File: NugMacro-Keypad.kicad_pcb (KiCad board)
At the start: 2 copper layers, 76.2 x 97.2 mm, 51 parts, among them J2 Conn_01x04, J3 Conn_01x04_Female_For_LCD, SW1 SW_Push, SW2 RotaryEncoder_Switch, U1 ATmega32U4-A, Y1 16MHz

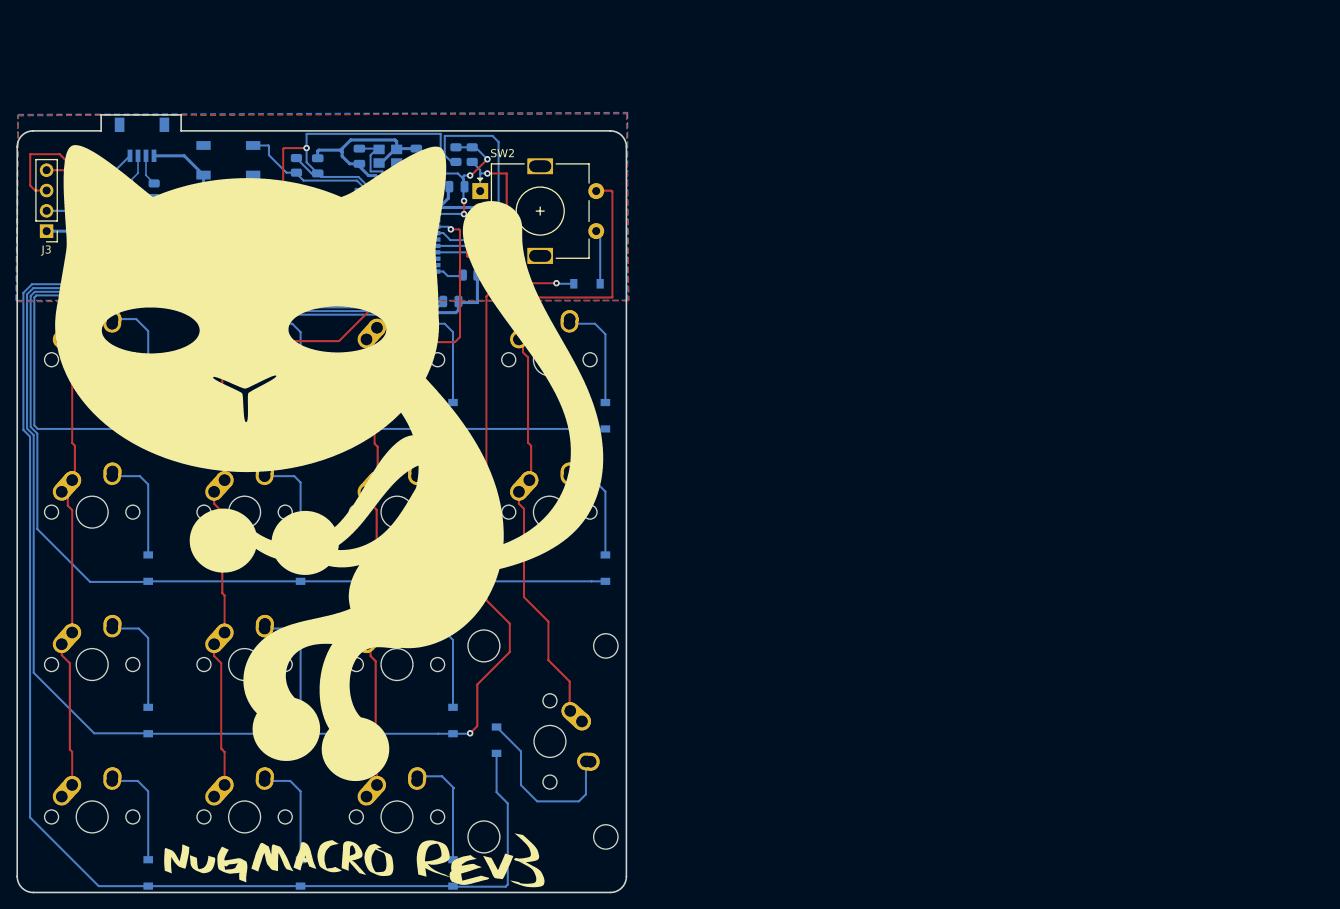
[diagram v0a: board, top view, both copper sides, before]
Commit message: ssilkcreen changess
added cat
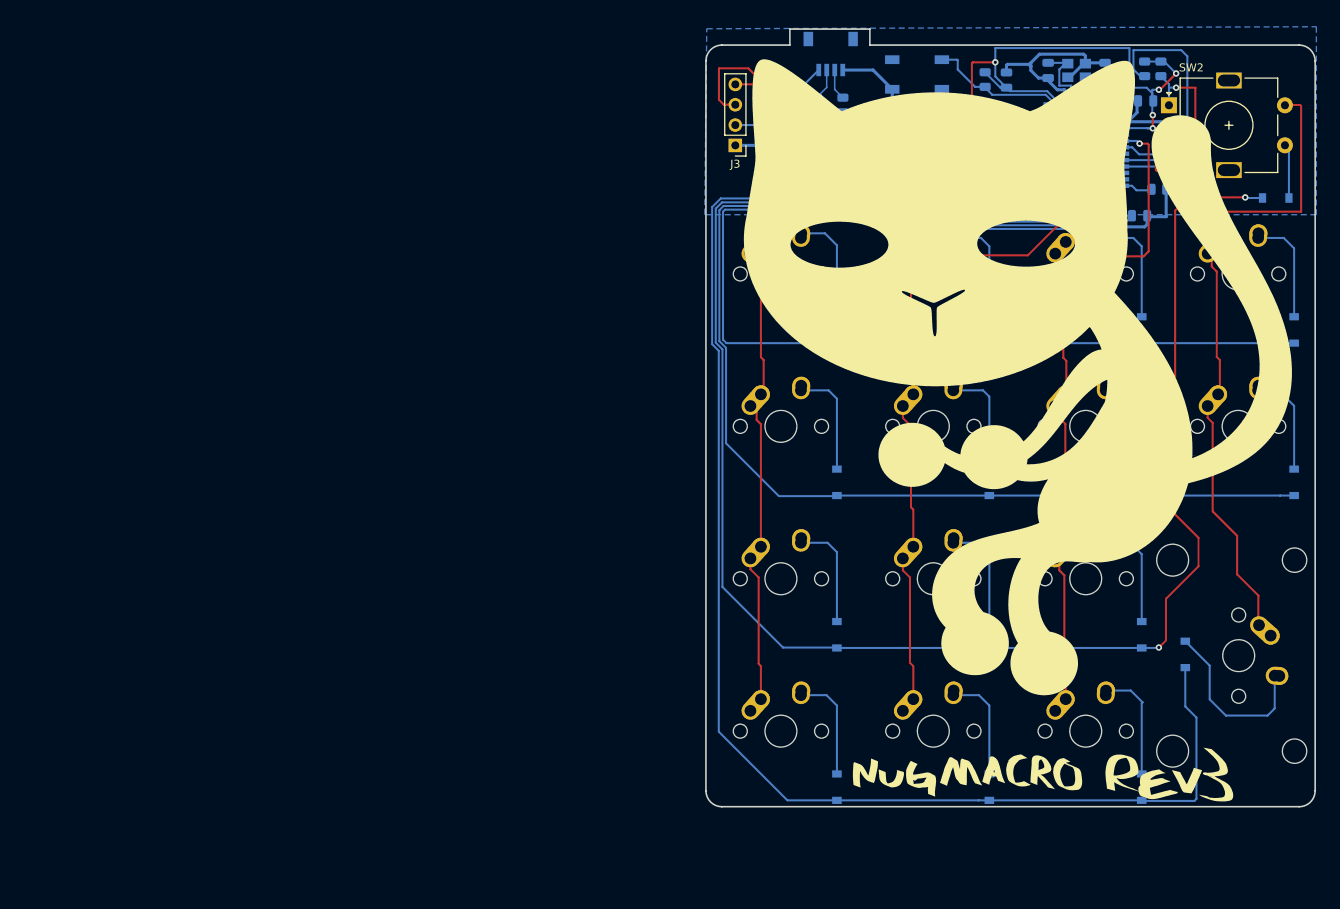
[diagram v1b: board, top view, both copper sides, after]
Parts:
- moved D13 86.8 mm to (178.1, 80.6)
- moved D14 86.8 mm to (178.1, 99.7)
- moved D15 86.8 mm to (164.5, 121.2)
- moved D6 86.8 mm to (140.0, 99.7)
- moved D8 86.8 mm to (140.0, 137.8)
- moved D9 86.8 mm to (159.0, 80.6)
- moved J3 86.8 mm to (108.2, 57.6)
- moved MX10 86.8 mm to (152.0, 92.7)
- moved MX11 86.8 mm to (152.0, 111.7)
- moved MX12 86.8 mm to (152.0, 130.8)
- moved MX13 86.8 mm to (171.1, 73.6)
- moved MX14 86.8 mm to (171.1, 92.7)
- moved MX15 86.8 mm to (171.1, 121.4)
- moved MX9 86.8 mm to (152.0, 73.6)
- moved R4 86.8 mm to (161.1, 63.1)
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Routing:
- removed copper zone on F.Cu, net GND

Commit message: done for now time to order
updated pcb grounds and silkscreen
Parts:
- moved R3 0.14 mm to (121.8, 52.5)
- moved R2 0.14 mm to (118.5, 52.5)
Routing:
- net GND: track 161.2 -> 105.5 mm, vias 0 -> 13
- added copper zone on F.Cu, net GND

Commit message: its done
yay
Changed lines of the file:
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@@
     (title "Nug Macro V3")
     (rev "V3")
-    (company "MIT Liscence")
+    (company "MIT License")
   )
   (layers
@@
   (segment (start 121.6274 48.9834) (end 123.19 50.546) (width 0.381) (layer "B.Cu") (net 2))
   (segment (start 149.3884 54.75847) (end 149.3884 52.91947) (width 0.381) (layer "B.Cu") (net 2))
-  (segment (start 139.3094 59.50847) (end 139.3044 59.51347) (width 0.381) (layer "B.Cu") (net 2))
   (segment (start 147.7884 64.31947) (end 147.7884 62.83547) (width 0.381) (layer "B.Cu") (net 2))
   (segment (start 162.0609 63.06447) (end 162.0609 64.5249) (width 0.381) (layer "B.Cu") (net 2))
@@
   (segment (start 156.63093 68.072) (end 158.877 68.072) (width 0.381) (layer "B.Cu") (net 2))
   (segment (start 159.6854 67.2636) (end 159.6854 66.36647) (width 0.381) (layer "B.Cu") (net 2))
-  (segment (start 143.8935 65.47747) (end 143.891 65.47497) (width 0.381) (layer "B.Cu") (net 2))
   (segment (start 142.0984 48.45947) (end 142.0984 47.57047) (width 0.381) (layer "B.Cu") (net 2))
   (segment (start 149.3884 52.91947) (end 149.3884 51.5984) (width 0.381) (layer "B.Cu") (net 2))
@@
   (segment (start 119.6274 50.47457) (end 118.491 51.61097) (width 0.2) (layer "B.Cu") (net 27))
   (segment (start 119.6274 48.15447) (end 119.6274 50.47457) (width 0.2) (layer "B.Cu") (net 27))
-  (segment (start 118.56903 51.61097) (end 118.3494 51.61097) (width 0.2) (layer "B.Cu") (net 27))
   (segment (start 136.5104 55.89847) (end 136.9454 55.89847) (width 0.254) (layer "F.Cu") (net 28))
   (segment (start 108.204581 49.955405) (end 111.202283 49.955405) (width 0.254) (layer "F.Cu") (net 28))

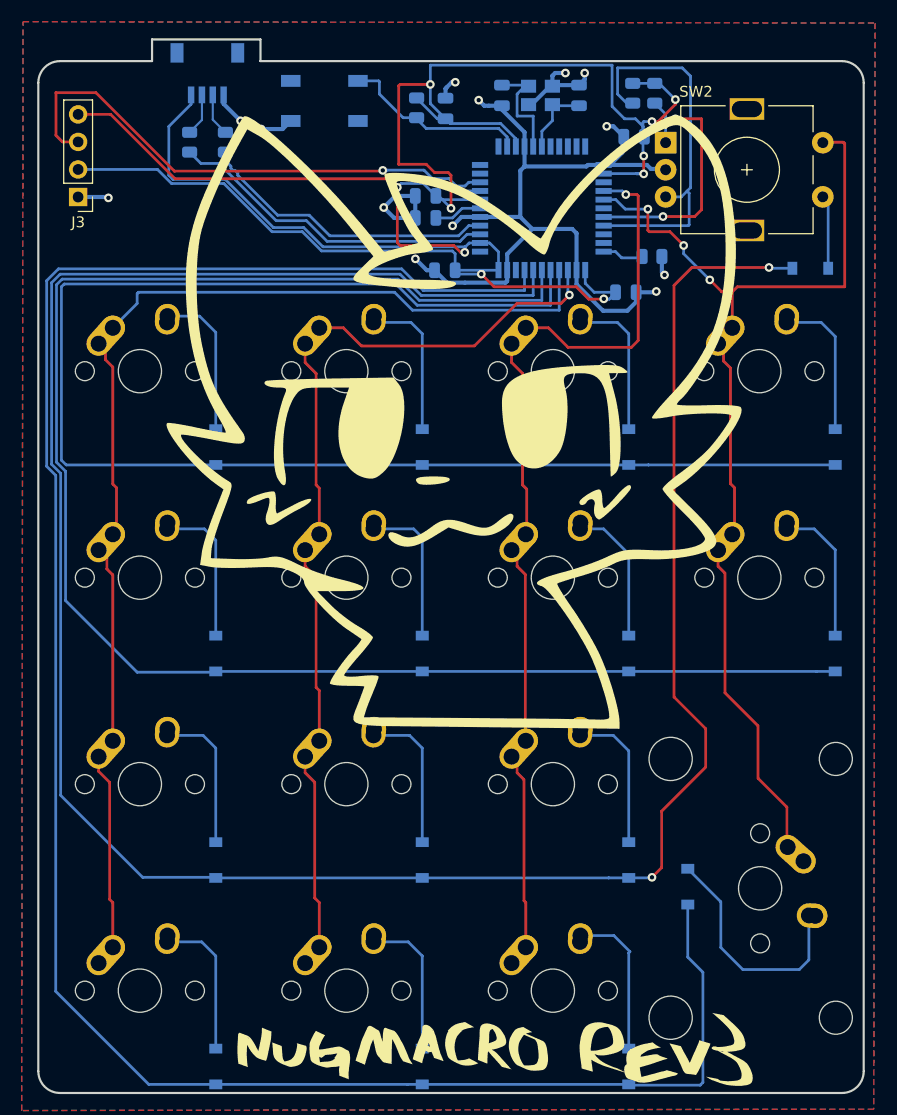
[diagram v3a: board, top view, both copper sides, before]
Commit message: starting rev 3 improvements
now that i have a working prototype making small changes, changed switches to mx only, and cleaned up some routing so far.
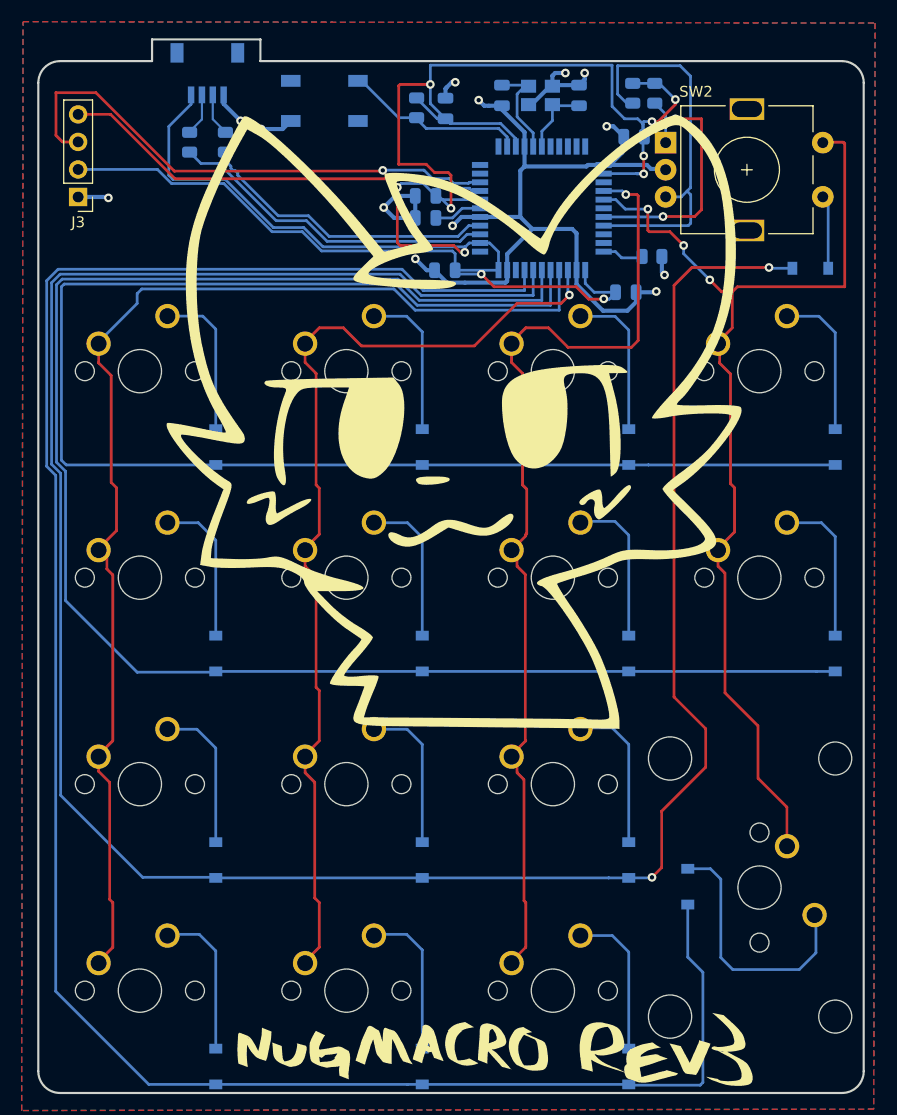
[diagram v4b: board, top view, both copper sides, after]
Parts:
- MX1, MX10, MX11, MX12, MX13, MX14, MX2, MX3, MX4, MX5, MX6, MX7, MX8, MX9: footprint MX_Alps_Hybrid:MX-1U-NoLED -> MX_Only:MXOnly-1U-NoLED
- MX15: footprint MX_Alps_Hybrid:MX-2U-NoLED -> MX_Only:MXOnly-2U-NoLED
- moved MX15 0.09 mm to (171.1, 121.3)
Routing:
- net COL0: track 102.1 -> 110.4 mm
- net COL2: track 82.6 -> 90.6 mm
- net COL1: track 82.5 -> 90.5 mm
- net COL3: track 94.5 -> 98.4 mm
- net Net-(D15-Pad2): track 22.0 -> 23.4 mm
- net XTAL2: track 10.6 -> 9.76 mm
- net RESET: track 17.5 -> 16.9 mm
- net Net-(D10-Pad2): track 13.0 -> 13.6 mm
